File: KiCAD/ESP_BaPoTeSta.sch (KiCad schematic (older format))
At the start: 27 parts, among them P1 Progr, P10 CONN_01X04, P13 CONN_01X03, P15 CONN_01X04, P2 Battery, P4 Upload, P5 Config, P9 CONN_01X04, Q1 IRLML6302, U1 MCP1700-330, U2 ESP-12

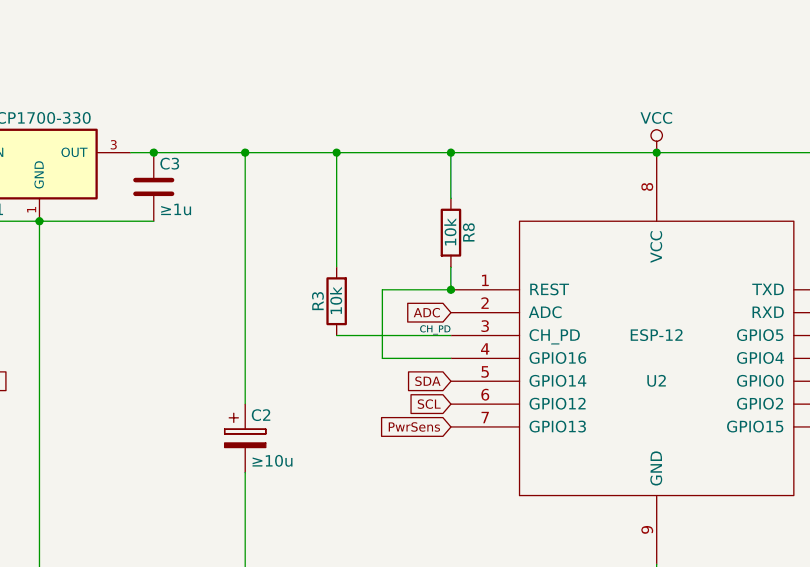
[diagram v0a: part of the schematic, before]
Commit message: ENH: PCB: cosmetic changes
label "RST" net
label pins of DHT header
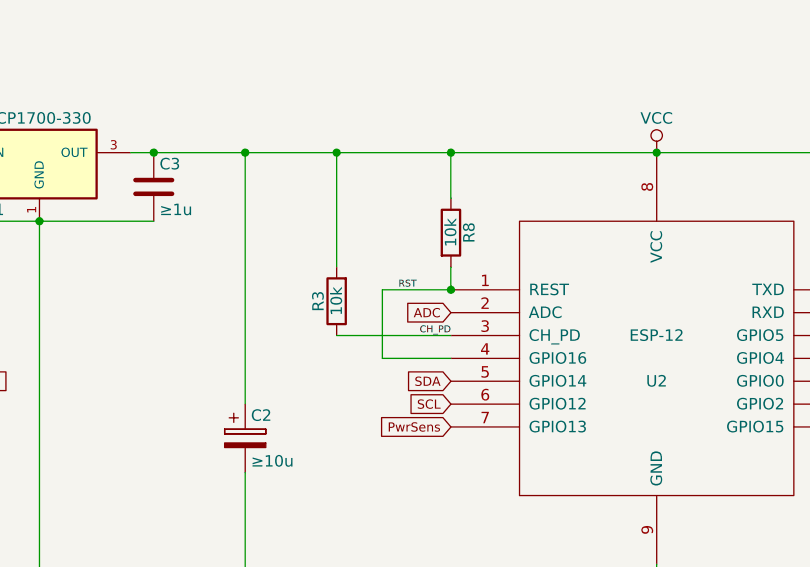
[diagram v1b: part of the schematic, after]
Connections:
- net RST: now reaches R8.2, U2.1 (REST), U2.4 (GPIO16)
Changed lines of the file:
@@
 	5650 6450 5850 6450
 Connection ~ 4050 2100
+Text Label 4800 2700 2    30   ~ 0
+RST
 $EndSCHEMATC

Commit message: ENH: PCB: use SOT-23 MCP1700
takes less space, easier to solder
obsoletes #21
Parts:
- U1: footprint TO_SOT_Packages_THT:TO-92_Inline_Wide -> TO_SOT_Packages_SMD:SOT-23_Handsoldering
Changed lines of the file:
@@
 F 0 "U1" H 2950 2350 50  0000 C CNN
 F 1 "MCP1700-330" H 2900 1950 50  0000 L CNN
-F 2 "TO_SOT_Packages_THT:TO-92_Inline_Wide" H 3150 2050 50  0001 C CIN
+F 2 "TO_SOT_Packages_SMD:SOT-23_Handsoldering" H 3150 2050 50  0001 C CIN
 F 3 "" H 3150 2150 50  0000 C CNN
 	1    3150 2150

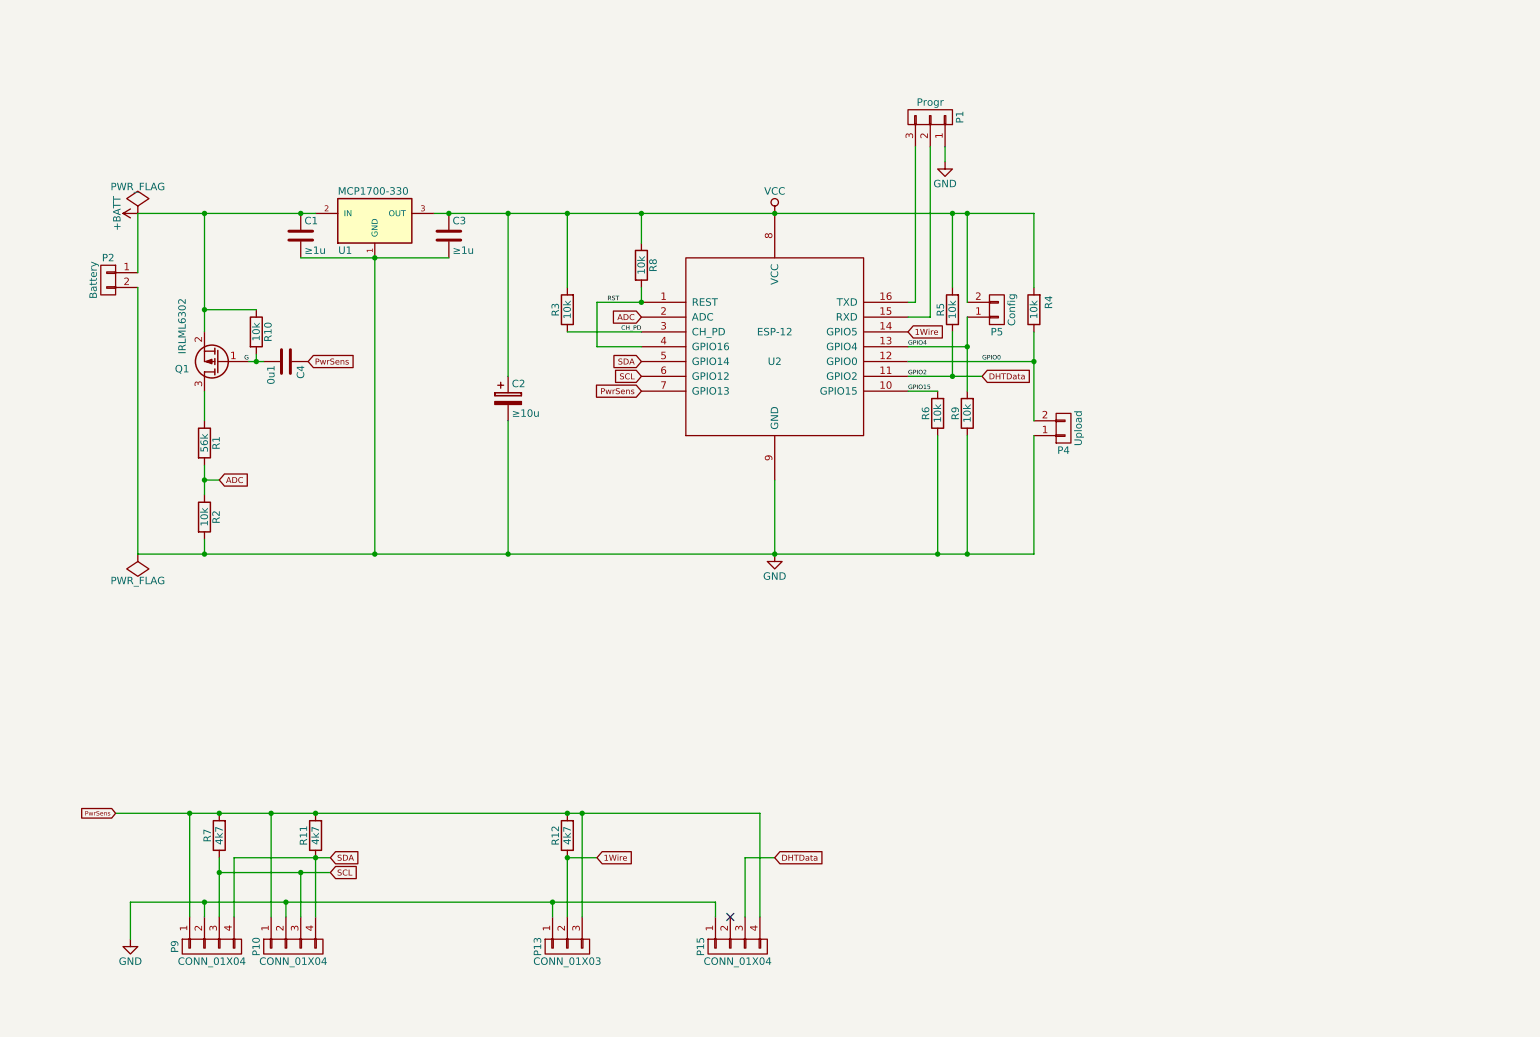
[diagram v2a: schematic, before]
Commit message: WIP: PCB: battery charger
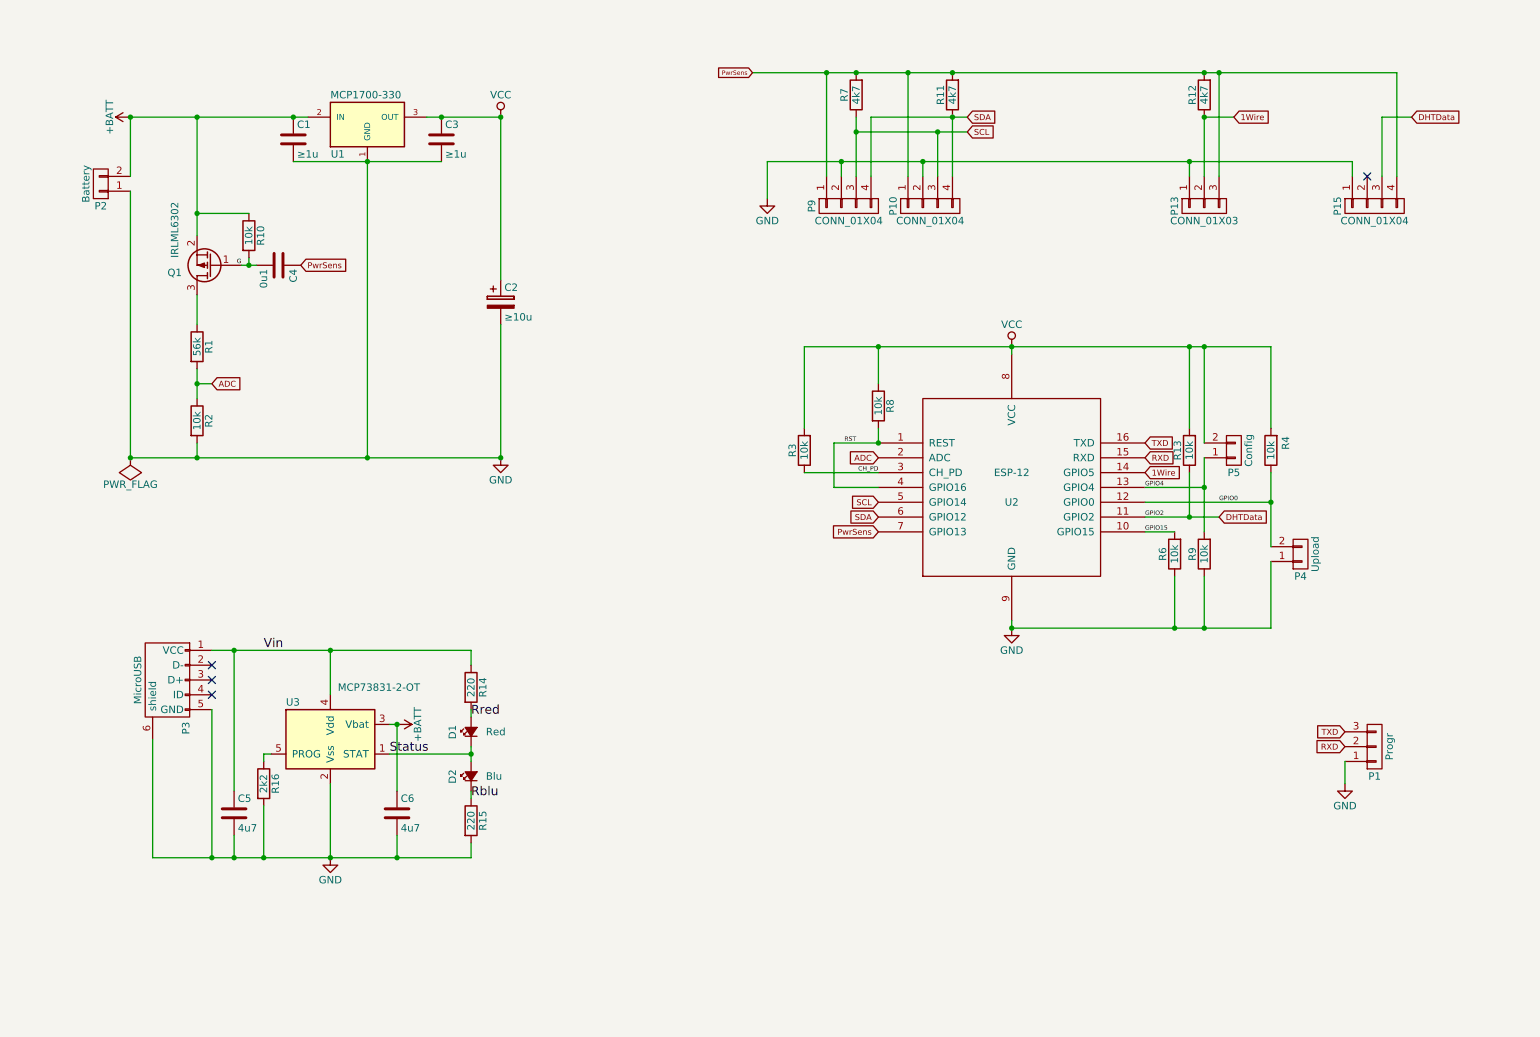
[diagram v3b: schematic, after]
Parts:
- added C5, C6: 4u7, Capacitors_SMD:C_1206_HandSoldering, symbol C
- added D1: Red, LEDs:LED_0805, symbol Led_Small
- added D2: Blu, LEDs:LED_0805, symbol Led_Small
- added P3: MicroUSB, Connect:USB_Micro-B, symbol USB_OTG
- added R14, R15: 220, Resistors_SMD:R_1206_HandSoldering, symbol R
- added R16: 2k2, Resistors_SMD:R_1206_HandSoldering, symbol R
- added U3: MCP73831-2-OT, TO_SOT_Packages_SMD:SOT-23-5, symbol MCP73831-2-OT
- renumbered R5 to R13
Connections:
- net +BATT: now also P2.2 (P2), C6.1, U3.3 (Vbat); no longer P2.1 (P1)
- net GND: now also P2.1 (P1), C5.2, C6.2, P3.5 (GND), P3.6 (shield), R15.2, R16.2, U3.2 (Vss); no longer P2.2 (P2)
- net SCL: now also U2.5 (GPIO14); no longer U2.6 (GPIO12)
- net SDA: now also U2.6 (GPIO12); no longer U2.5 (GPIO14)
- net RXD: now reaches P1.2 (P2), U2.15 (RXD)
- net TXD: now reaches P1.3 (P3), U2.16 (TXD)
- new net: R16.1, U3.5 (PROG)
- new net Rblu: D2.1 (K), R15.1
- new net Rred: D1.2 (A), R14.2
- new net Status: D1.1 (K), D2.2 (A), U3.1 (STAT)
- new net Vin: C5.1, P3.1 (VCC), R14.1, U3.4 (Vdd)
- no-connect marks 1 -> 4
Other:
- moved on the sheet: C1, C2, C3, C4, P1, P10, P13, P15, P2, P4, P5, P9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

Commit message: WIP: PCB: redesign nearly finished
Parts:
- removed C6: 4u7, Capacitors_SMD:C_1206_HandSoldering, symbol C
- P2: footprint Pin_Headers:Pin_Header_Angled_1x02 -> Pin_Headers:Pin_Header_Straight_1x02
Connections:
- net +BATT: now also P2.1 (P1); no longer P2.2 (P2)
- net GND: now also P2.2 (P2); no longer P2.1 (P1)
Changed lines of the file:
@@
 F 0 "P2" H 1300 2050 50  0000 C CNN
 F 1 "Battery" V 1400 1900 50  0000 C CNN
-F 2 "Pin_Headers:Pin_Header_Angled_1x02" H 1300 1900 50  0001 C CNN
+F 2 "Pin_Headers:Pin_Header_Straight_1x02" H 1300 1900 50  0001 C CNN
 F 3 "" H 1300 1900 50  0000 C CNN
 	1    1300 1900
-	-1   0    0    1
+	-1   0    0    -1
 $EndComp
 $Comp
@@
 	1    0    0    -1
 $EndComp
-$Comp
-L C C6
-U 1 1 5829CE52
-P 3300 6150
-F 0 "C6" H 3325 6250 50  0000 L CNN
-F 1 "4u7" H 3325 6050 50  0000 L CNN
-F 2 "Capacitors_SMD:C_1206_HandSoldering" H 3338 6000 50  0001 C CNN
-F 3 "" H 3300 6150 50  0000 C CNN
-	1    3300 6150
-	1    0    0    -1
-$EndComp
-Wire Wire Line
-	3300 6000 3300 5550
-Connection ~ 3300 5550
-Wire Wire Line
-	3300 6300 3300 6450
-Connection ~ 3300 6450
 Wire Wire Line
 	2200 6300 2200 6450

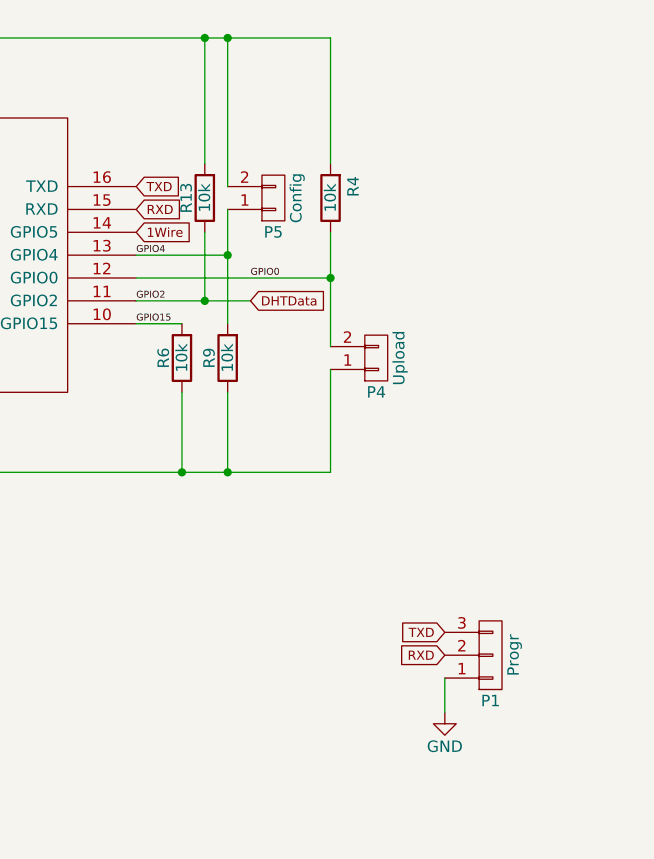
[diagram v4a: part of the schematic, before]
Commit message: DOC: PCB: silkscreen improvements
Fix size/position of labels
swap GPIO 4<->5 labels
add header diagram
fix voltage labels (ESP needs 2.5V in, so 3.0V battery is ok)
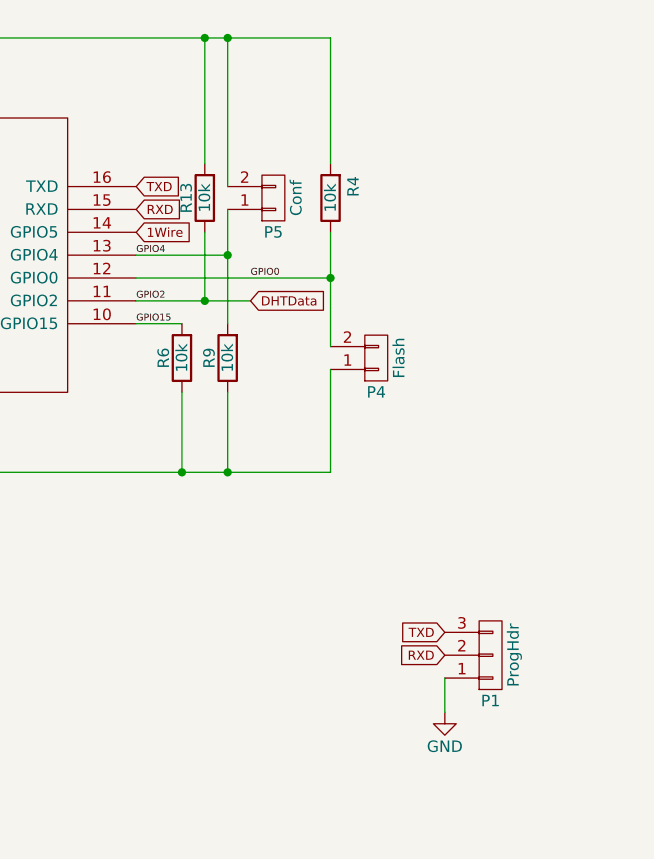
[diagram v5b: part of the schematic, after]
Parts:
- P1: value Progr -> ProgHdr
- P4: value Upload -> Flash
- P5: value Config -> Conf
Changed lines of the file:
@@
 P 9900 5700
 F 0 "P1" H 9900 5900 50  0000 C CNN
-F 1 "Progr" V 10000 5700 50  0000 C CNN
+F 1 "ProgHdr" V 10000 5700 50  0000 C CNN
 F 2 "Pin_Headers:Pin_Header_Straight_1x03" H 9900 5700 50  0001 C CNN
 F 3 "" H 9900 5700 50  0000 C CNN
@@
 P 9400 4400
 F 0 "P4" H 9400 4550 50  0000 C CNN
-F 1 "Upload" V 9500 4400 50  0000 C CNN
+F 1 "Flash" V 9500 4400 50  0000 C CNN
 F 2 "Pin_Headers:Pin_Header_Straight_1x02" H 9400 4400 50  0001 C CNN
 F 3 "" H 9400 4400 50  0000 C CNN
@@
 P 8950 3700
 F 0 "P5" H 8950 3850 50  0000 C CNN
-F 1 "Config" V 9050 3700 50  0000 C CNN
+F 1 "Conf" V 9050 3700 50  0000 C CNN
 F 2 "Pin_Headers:Pin_Header_Straight_1x02" H 8950 3700 50  0001 C CNN
 F 3 "" H 8950 3700 50  0000 C CNN

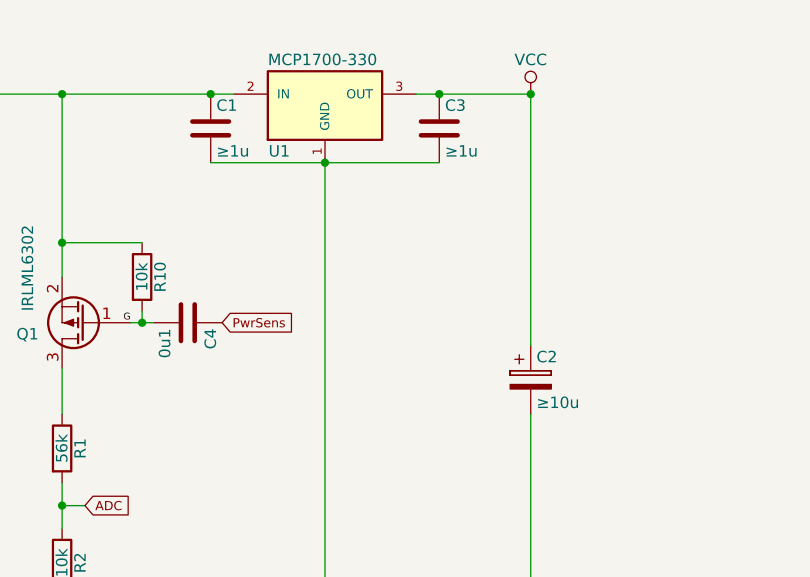
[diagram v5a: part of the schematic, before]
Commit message: ENH: Use SMD capacitor as C2
fixes #24
fixes #30
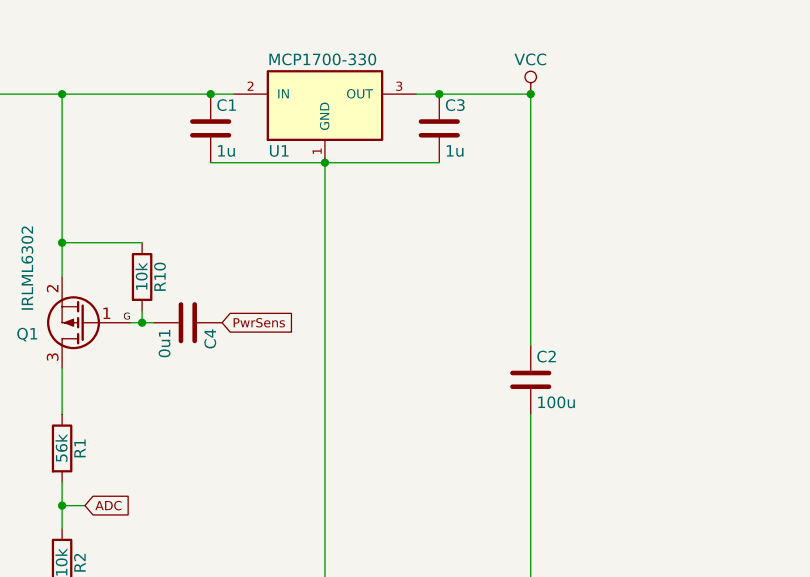
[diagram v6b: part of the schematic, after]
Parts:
- removed C2: ≥10u, Capacitors_ThroughHole:C_Radial_D5_L11_P2.5, symbol CP
- added C2: 100u, Capacitors_SMD:C_1206_HandSoldering, symbol C
- C1, C3: value ≥1u -> 1u
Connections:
- net GND: now also C2.2
- net VCC: now also C2.1
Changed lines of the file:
@@
 P 2600 1600
 F 0 "C1" H 2625 1700 50  0000 L CNN
-F 1 "≥1u" H 2625 1500 50  0000 L CNN
+F 1 "1u" H 2625 1500 50  0000 L CNN
 F 2 "Capacitors_SMD:C_1206_HandSoldering" H 2638 1450 50  0001 C CNN
 F 3 "" H 2600 1600 50  0000 C CNN
@@
 P 3600 1600
 F 0 "C3" H 3625 1700 50  0000 L CNN
-F 1 "≥1u" H 3625 1500 50  0000 L CNN
+F 1 "1u" H 3625 1500 50  0000 L CNN
 F 2 "Capacitors_SMD:C_1206_HandSoldering" H 3638 1450 50  0001 C CNN
 F 3 "" H 3600 1600 50  0000 C CNN
 	1    3600 1600
-	1    0    0    -1
-$EndComp
-$Comp
-L CP C2
-U 1 1 56929DFC
-P 4000 2700
-F 0 "C2" H 4025 2800 50  0000 L CNN
-F 1 "≥10u" H 4025 2600 50  0000 L CNN
-F 2 "Capacitors_ThroughHole:C_Radial_D5_L11_P2.5" H 4038 2550 50  0001 C CNN
-F 3 "" H 4000 2700 50  0000 C CNN
-	1    4000 2700
 	1    0    0    -1
 $EndComp
@@
 	2200 6000 2200 5050
 Connection ~ 2200 5050
+$Comp
+L C C2
+U 1 1 583F3D5B
+P 4000 2700
+F 0 "C2" H 4025 2800 50  0000 L CNN
+F 1 "100u" H 4025 2600 50  0000 L CNN
+F 2 "Capacitors_SMD:C_1206_HandSoldering" H 4038 2550 50  0001 C CNN
+F 3 "" H 4000 2700 50  0000 C CNN
+	1    4000 2700
+	1    0    0    -1
+$EndComp
 $EndSCHEMATC
